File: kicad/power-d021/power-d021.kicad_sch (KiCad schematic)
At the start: 29 parts, among them J301 T1_SECONDARY, J302 PVDD_TO_CORE, J303 AUX_TO_CORE, U302 LM5164DDA, U303 TPS3700DDC

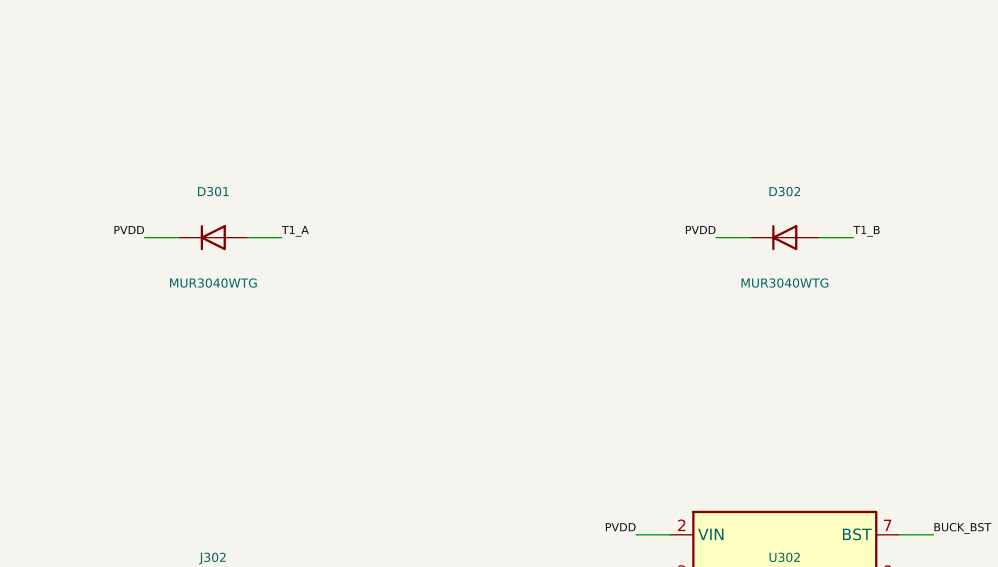
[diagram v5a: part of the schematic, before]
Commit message: feat(pcb): placa única D-030 com potência fechada e regras pragmáticas
- revoga D-029 (Rev A/Rev B) e remove kicad/rev-a-bench
- J301 JST B3P-VH (manual PS28 p.14), D301/D302 P600J, C301/C302 em footprint D30,
  F301 Littelfuse 02186.3MXP; R201 DIN0617 vertical
- ERC: pinos PBTL paralelos passive e TP101 MONO_IN (de fix/pcb-route-drc-erc)
- system-candidate regenerada: 205 footprints, ERC 0, DRC 0, paridade 0,
  471 conexões para rota manual; autoroute de estudo descartado; galeria 3D refeita
- AGENTS.md/safety/PLANNING: política de evidência pragmática e Done objetivo
- tasks SETUP-003, PCB-003, PWR-001, ELEC-001 e SYS-001 concluídas
- roteiro de medidas restantes em mechanical/measurement-request.md
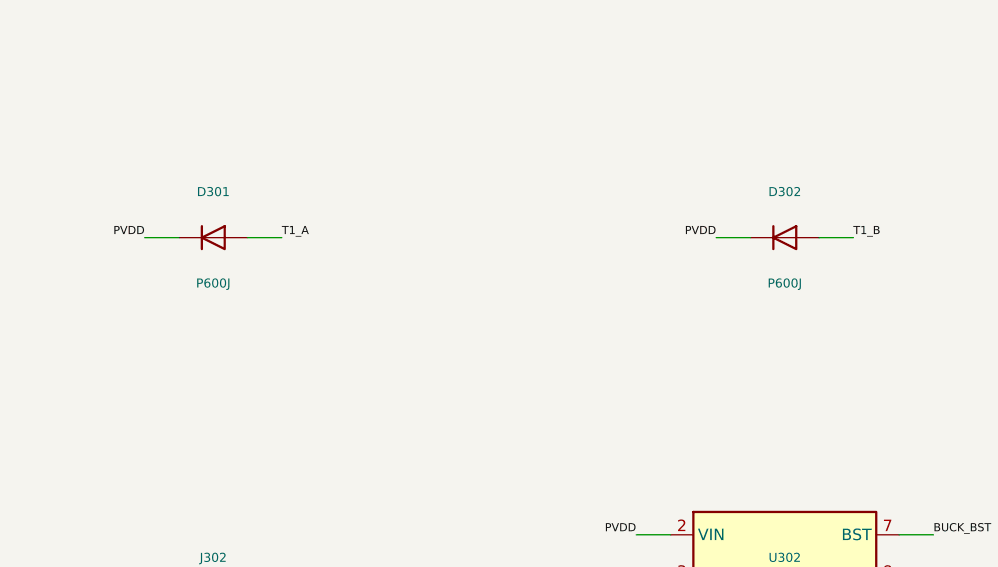
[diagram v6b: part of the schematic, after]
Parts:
- C301, C302: footprint Capacitor_THT:CP_Radial_D25.0mm_P10.00mm_SnapIn -> Capacitor_THT:CP_Radial_D30.0mm_P10.00mm_SnapIn; MPN Rubycon 63USC4700MEFCSN30X30 (LCSC C1498587): 4700 uF/63 V, 3.49 A rms @120 Hz, D30xL30, 3000 h @85 C (D-025) -> Rubycon 63USC4700MEFCSN30X30 (LCSC C1498587): 4700 uF/63 V, 3.49 A rms @120 Hz, D30xL30; with C14/C15 3000 uF >= OEM 2x6800 uF/50 V margin on voltage (D-030)
- D301, D302: value MUR3040WTG -> P600J; MPN onsemi MUR3040WTG (MUR3020WT/D Rev.7): VRRM 400 V, IF(AV) 1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 -> P600J (Diodes Inc./Vishay), R-6 axial: 600 V, 6 A, IFSM 400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
- F301: MPN Time-lag (T) 5x20 mm; I2t melt above measured inrush, >=63 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 -> Littelfuse 02186.3MXP, 218 series T 6.3 A 5x20 mm, in Schur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
- J301: MPN JST VH SVH-41T-P1.1 terminals (20-16 AWG, 10 A) on VHR-4N h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 -> JST B3P-VH(LF)(SN) header 3 pos 3.96 mm; mates OEM T1 harne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
